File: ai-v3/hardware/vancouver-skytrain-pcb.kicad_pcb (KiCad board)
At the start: 2 copper layers, 150 x 150 mm, 85 parts, among them SW1 TS-1187A-B-A-B, SW2 TS-1187A-B-A-B, SW3 TS-1187A-B-A-B, SW4 TS-1187A-B-A-B, U1 XIAO-RP2040-DIP

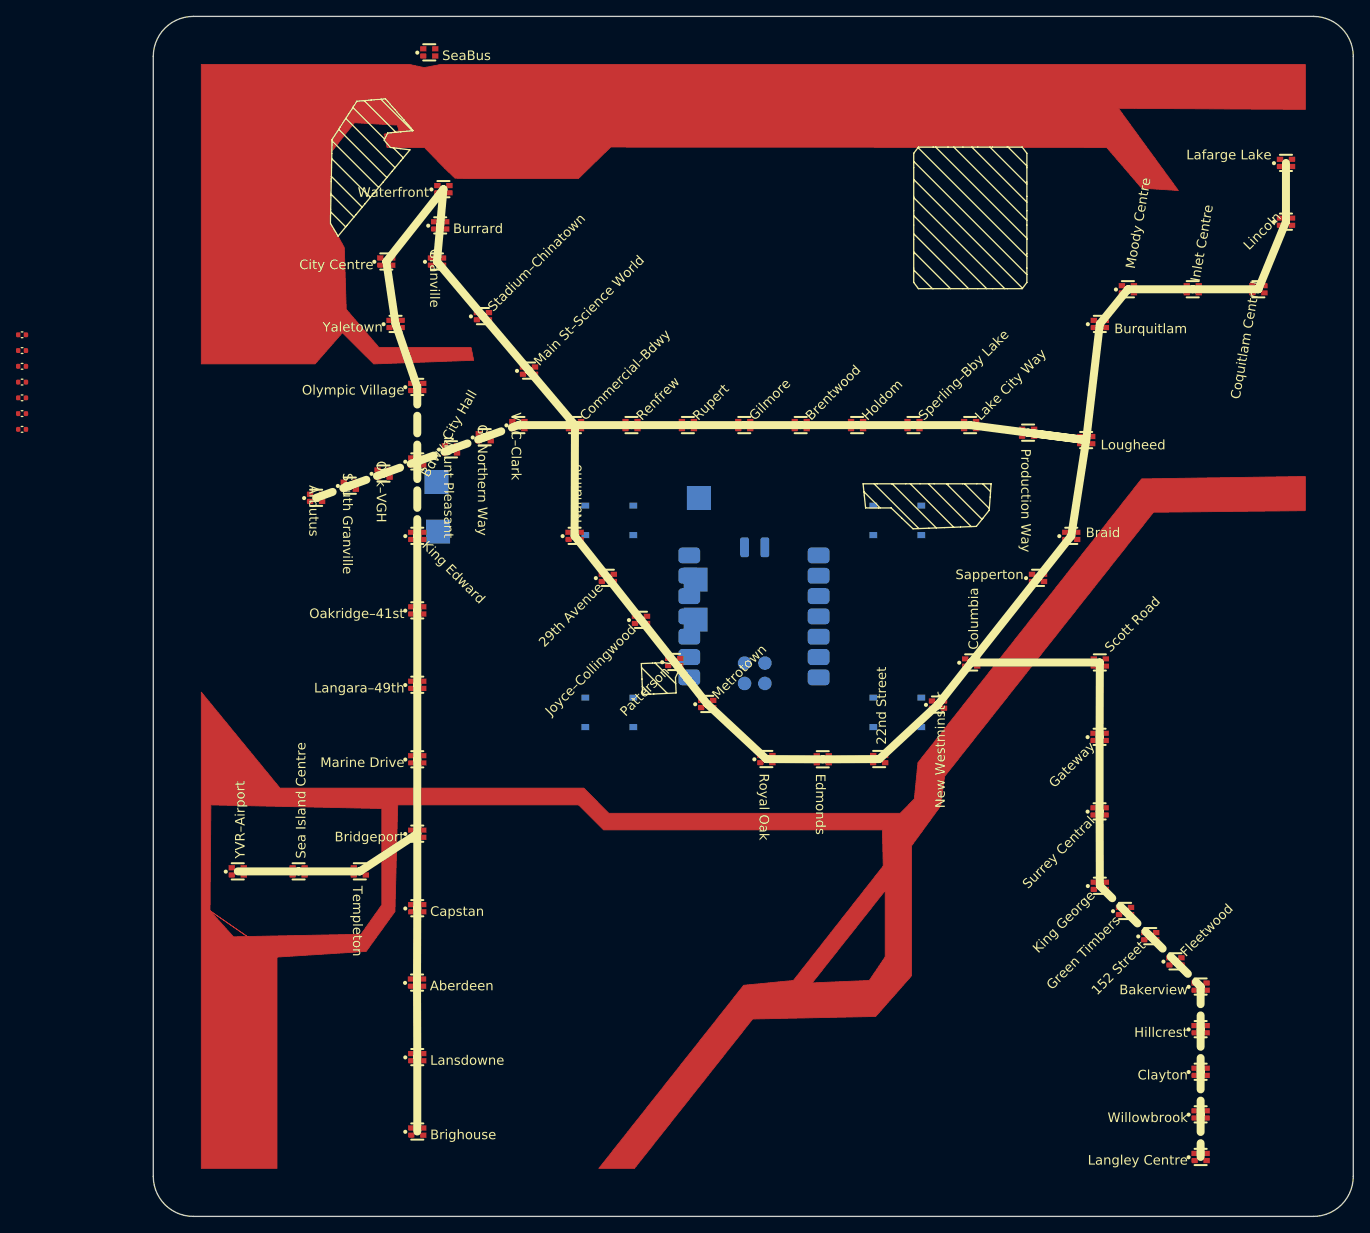
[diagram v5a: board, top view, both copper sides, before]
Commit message: ai-v3: fix vertical stretch, auto-optimize label placement
- build_vancouver_json.py / build_geo.py: replaced independent x/y
  scaling (which stretched the network to fill the square board,
  distorting every real angle from the PDF) with one uniform scale
  factor sized to the page width, top-aligned. The source map is
  wider than tall, so this leaves blank canvas at the bottom instead
  of stretching content vertically - proportions now match the PDF
  exactly except for the one physically-required exception: Waterfront/
  Burrard/Granville were nudged apart by ~0.4mm each (preserving their
  real line direction) since the real map draws them closer together
  than a 2.5mm LED pitch can physically be soldered.
- tools/auto_label.py: brute-forces every label angle/anchor
  combination per flagged station and keeps whichever has the fewest
  real collisions (label-label/label-dot/label-line - not label-geo,
  which is expected for genuinely coastal stations). Replaces the
  slow one-station-at-a-time manual tuning from the last two rounds.
  Constrained to angle in [-90, 90]: wider angles render KiCad gr_text
  upside-down/mirrored (rotation is rigid, no auto-flip), which the
  first brute-force pass didn't know about and produced 8 backwards
  labels (Sapperton, Lafarge Lake, Coquitlam Centre, South Granville,
  King Edward, Oakridge, Mount Pleasant, Inlet Centre) - caught by
  eye on the render and fixed by re-running within the safe range.
- Net result: Broadway-City Hall vs Mount Pleasant (the requested
  fix) and every other real label collision from the last pass is
  now resolved; only expected label-near-water/park proximity
  remains (19 of those, all coastal stations).
- Re-verified via kicad-cli: clearance/copper_edge_clearance still 0;
  re-rendered board-top.png/board-bottom.png against the corrected
  proportions.

Co-Authored-By: Claude Fable 5 <noreply@anthropic.com>
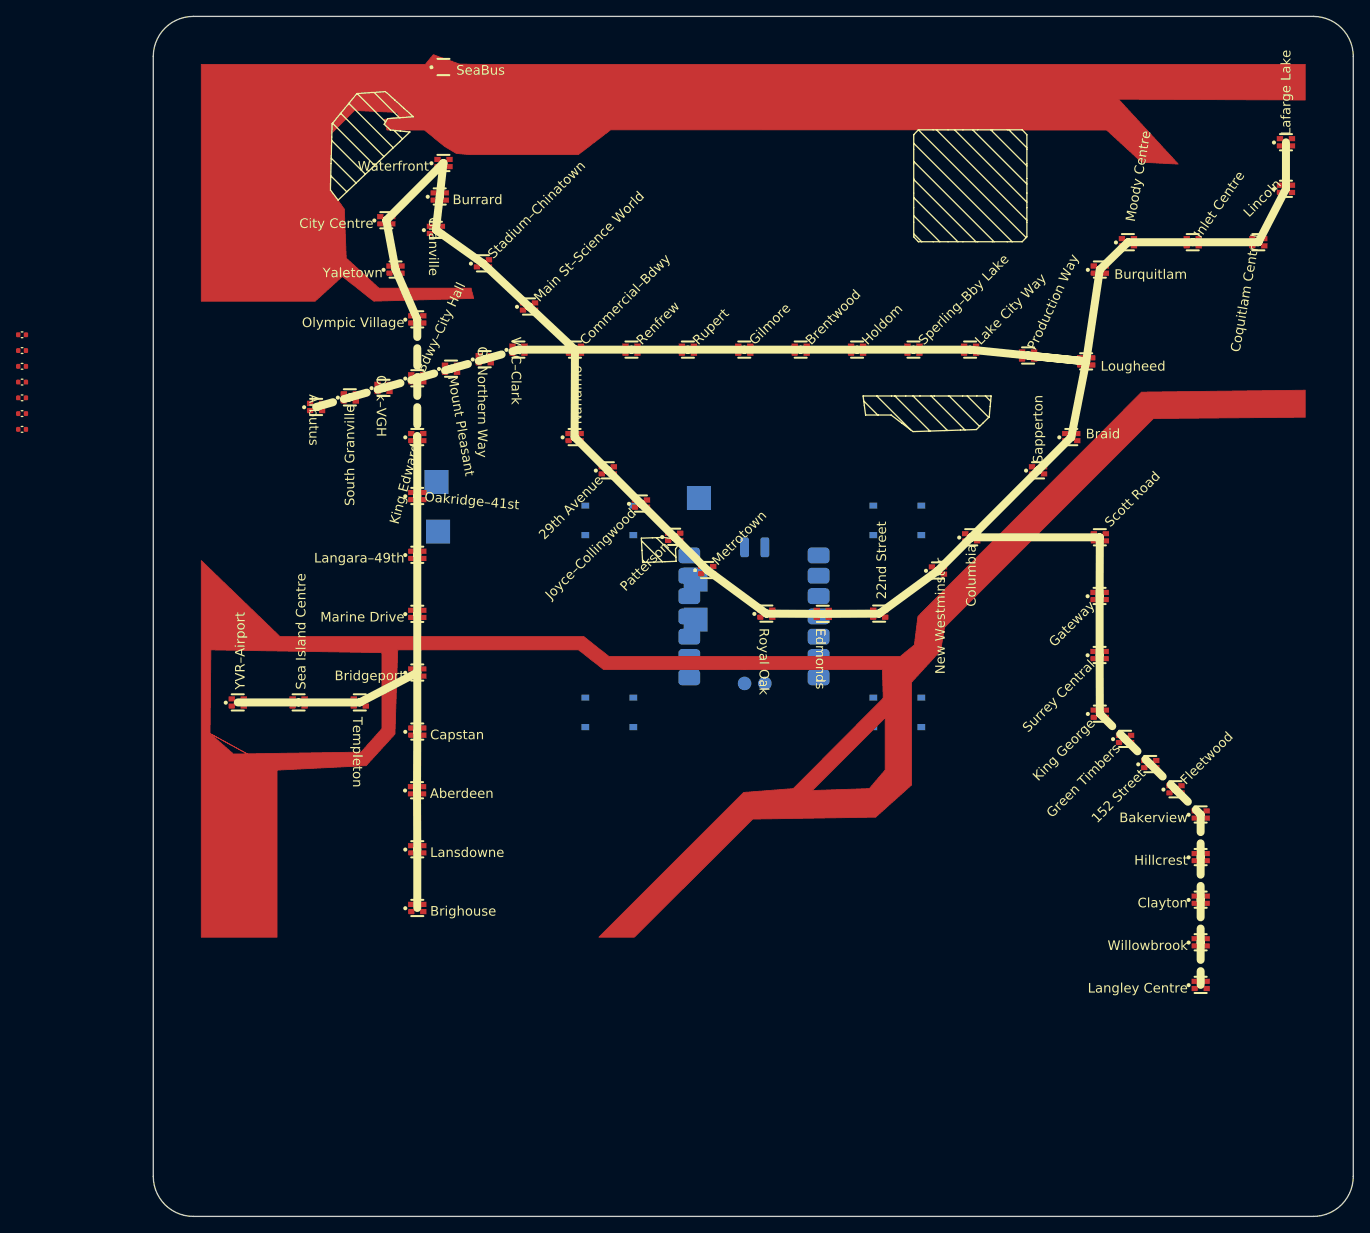
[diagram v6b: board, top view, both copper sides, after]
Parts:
- moved LED68 27.9 mm to (33.0, 111.5)
- moved LED67 26.0 mm to (33.0, 104.1)
- moved LED66 24.0 mm to (33.0, 96.7)
- moved LED65 22.1 mm to (33.0, 89.4)
- moved LED22 21.5 mm to (121.5, 90.3)
- moved LED24 21.5 mm to (127.8, 96.6)
- moved LED25 21.5 mm to (130.9, 99.8)
- moved LED27 21.5 mm to (130.9, 110.4)
- moved LED28 21.5 mm to (130.9, 115.7)
- moved LED21 21.5 mm to (118.3, 87.2)
- moved LED23 21.5 mm to (124.6, 93.5)
- moved LED26 21.5 mm to (130.9, 105.1)
- moved LED29 21.5 mm to (130.9, 121.1)
- moved LED62 21.1 mm to (25.8, 85.8)
- moved LED63 21.1 mm to (18.2, 85.8)
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
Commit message: ai-v3: straighten Broadway corridor, extend water to left edge, fix SeaBus
- build_vancouver_json.py: the Broadway corridor (real Millennium
  trunk VCC-Clark..Lake City Way plus its future westward extension
  to Arbutus) is one straight street in reality - the row now stays
  on a single flat line at Broadway-City Hall's y (its fixed
  interchange point on the Canada Line column) instead of sloping
  down to meet it. Arbutus..VCC-Clark is computed as one continuous
  6-gap sequence with a single step size derived from the two real
  traced anchors (Broadway-City Hall, VCC-Clark), replacing the
  earlier two independently-anchored half-chains that could overlap.
- build_geo.py: the source PDF only details coastline near stations -
  west of the Cambie corridor (Point Grey/English Bay, no stations
  there) it's flat land colour, leaving the board's left edge
  landlocked for a stretch. Added a west-coast patch strip (unioned
  with the traced water before the hole/simplify step) connecting
  the two traced water pieces along the left margin, matching real
  Vancouver geography (open water the whole way down that coast).
- build_vancouver_json.py: SeaBus was landing inside the water fill
  since it was placed at a fixed offset north of Waterfront without
  checking the actual coastline. Replaced with a grid search for the
  closest point on the land side of the traced water polygon that
  also clears LED pitch from both Waterfront and Burrard.
- Codified the Waterfront/Burrard/Granville LED-pitch nudge (from
  two sessions ago) directly into the script instead of a one-off
  manual edit, so it survives a re-trace.
- auto_label.py: find_station() now resolves extras (SeaBus) as well
  as named stations, since the geometry changes moved it enough to
  need a label re-check too.
- Fixed the handful of label collisions these geometry changes
  introduced as a side effect (Waterfront/SeaBus, Production
  Way/Lake City Way, Mount Pleasant/Great Northern Way/Oakridge) -
  s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
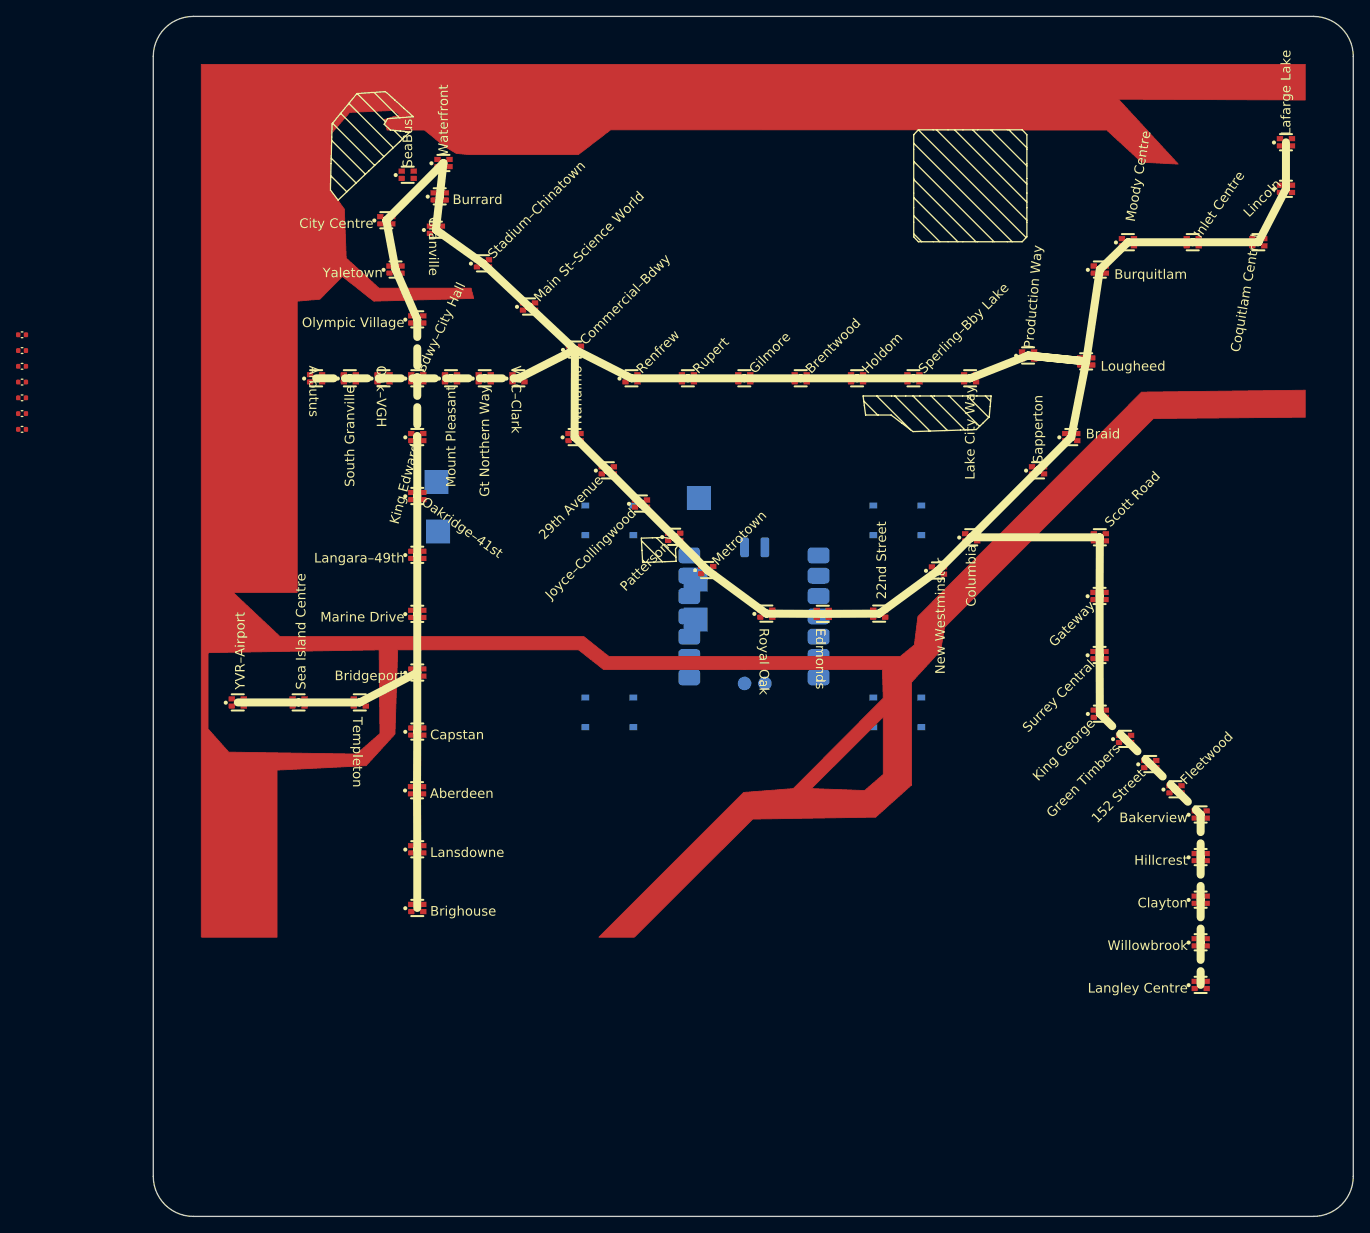
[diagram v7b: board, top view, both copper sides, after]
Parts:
- moved LED1 14.2 mm to (31.8, 19.8)
- moved LED40 3.59 mm to (102.1, 45.2)
- moved LED41 3.59 mm to (95.0, 45.2)
- moved LED42 3.59 mm to (88.0, 45.2)
- moved LED43 3.59 mm to (80.9, 45.2)
- moved LED44 3.59 mm to (73.9, 45.2)
- moved LED45 3.59 mm to (66.8, 45.2)
- moved LED46 3.59 mm to (59.8, 45.2)
- moved LED47 3.59 mm to (45.6, 45.2)
- moved LED53 3.59 mm to (20.4, 45.2)
- moved LED48 2.39 mm to (41.4, 45.2)
- moved LED52 2.38 mm to (24.6, 45.2)
- moved LED49 1.20 mm to (37.2, 45.2)
- moved LED51 1.20 mm to (28.8, 45.2)

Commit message: ai-v3: restore Point Grey peninsula, bump version, fix pad overlap
- build_geo.py: the west-coast water patch from two sessions ago
  paved straight over Point Grey (the real UBC/Kitsilano peninsula,
  right at Arbutus's latitude) with a flat rectangle, clipping it at
  the board edge instead of showing it. Carved a rounded cape shape
  back out of the patch - a real, well-known landform (not traced,
  since no station sits on it to anchor a PDF trace to, but not
  invented either).
- hardware/vancouver-skytrain-pcb.kicad_pcb: bumped the back-silk
  version text from 2025-Nov-29 (stale, left over from v2) to
  2026-Aug-31.
- tools/reposition_board.py: three test points (GND/+5V/LED_IN) were
  hand-placed leftovers from v2's original 100x82.9mm layout,
  positioned relative to U1's old off-centre spot - they never moved
  when U1 got recentred for the 150mm board, landing inside its
  courtyard (confirmed by courtyards_overlap/shorting_items DRC
  categories, both now gone). Reference-only matching can't fix this
  since a second, unrelated '+5V' test point exists elsewhere on the
  board - keyed these three by uuid instead and placed them just
  outside the XIAO courtyard, clear of the SW1/SW2 buttons too.
- Re-verified via kicad-cli: clearance/copper_edge_clearance still 0,
  courtyards_overlap and shorting_items both dropped to 0; re-rendered
  board-top.png/board-bottom.png.

Co-Authored-By: Claude Fable 5 <noreply@anthropic.com>
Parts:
- moved LED_IN 5.20 mm to (63.0, 60.2)
- moved +5V 4.80 mm to (63.0, 75.4)
- moved GND 4.80 mm to (63.0, 70.4)
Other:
- board text added: "Vancouver Skytrain Github.com/Funvill/Vancouver-Skytrain-PCB Version: 2026-Aug-31"
- board text removed: "Vancouver Skytrain Github.com/Funvill/Vancouver-Skytrain-PCB Version: 2025-Nov-29"
